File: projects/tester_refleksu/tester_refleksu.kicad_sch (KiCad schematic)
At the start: 25 parts, among them J1 +, J2 −, SW1 SW_Push_4P, SW2 SW_Push_4P, T1 BC548, T2 BC548, T3 BC557

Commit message: tester_refleksu_r2
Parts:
- added C3: 10μF, VeeCad:RA1_2, symbol Custom_Generic:C_Polarized
- added C4: 1nF, symbol *Custom_Generic:C
- added D4, D5: 4148, symbol *Custom_Generic:D
- added D7: 3V3, symbol *Custom_Generic:D_zener
- added R12, R15, R16: 10kΩ, VeeCad:AX3_1N, symbol Custom_Generic:R
- added R13, R14: 100kΩ, VeeCad:AX3_1N, symbol Custom_Generic:R
- added R17, R20, R21, R22: 1kΩ, VeeCad:AX3_1N, symbol Custom_Generic:R
- added R18, R19: 1kΩ, VeeCad:VERTAX_1N_180, symbol Custom_Generic:R
- added R23: 47kΩ, VeeCad:AX3_1N, symbol Custom_Generic:R
- added T4, T5, T6: 2n7000, symbol *Custom_Generic:NMOS_SGD
- added T7, T8, T9: BC548, VeeCad:TO92, symbol Custom_Generic:NPN_BJT_CBE
- added Y1: 3V, symbol *Custom_Generic:Buzzer_Magnetic_Active
- D1: value R -> Gr
- D2, D3: value Y -> Bl
- R8, R9: value 10kΩ -> 82kΩ
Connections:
- net GNDD: now also D7.2 (A), R17.1, R20.2, R21.2, T7.3 (E), T8.3 (E), Y1.2
- net VCC: now also R12.1, R13.1, R15.1, R22.2, T9.1 (C)
- net at D2.2 (A), D3.2 (A): now also R7.2; no longer R7.1
- net at R6.1, T3.1 (C): now also R7.1; no longer R7.2
- net at R10.2, TY2.2 (G): now also T4.1 (S); no longer SW2.1 (1A), SW2.3 (1B)
- net at R11.2, TY1.2 (G): now also T5.1 (S); no longer SW1.1 (1A), SW1.3 (1B)
- net at C2.2 (+), R4.2, T2.1 (C): now also R23.1
- new net: R23.2, T6.1 (S)
- new net: D4.1 (K), D5.1 (K), R21.1, T6.2 (G)
- new net: C4.2, T6.3 (D)
- new net: R19.2, SW2.1 (1A)
- new net: D5.2 (A), SW2.3 (1B)
- new net: R22.1, SW1.3 (1B), SW2.4 (2B)
- new net: D7.1 (K), R16.2, T9.2 (B)
- new net: T9.3 (E), Y1.1
- new net: R17.2, R18.1, T4.2 (G)
- new net: R9.1, T4.3 (D)
- new net: C3.1 (-), C4.1, R13.2, T8.2 (B)
- new net: R18.2, SW1.2 (2A)
- new net: D4.2 (A), SW1.4 (2B)
- new net: C3.2 (+), R12.2, T7.1 (C)
- new net: R14.2, R15.2, R16.1, T8.1 (C)
- new net: R8.2, T5.3 (D)
- new net: R14.1, T7.2 (B)
- new net: R19.1, R20.1, T5.2 (G)
- now unconnected: SW2.2 (2A)
- no-connect marks 0 -> 2
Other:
- note removed: "9...12V"
- moved on the sheet: C1, C2, D1, D2, D3, R1, R10, R11, R2, R3, R4, R5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

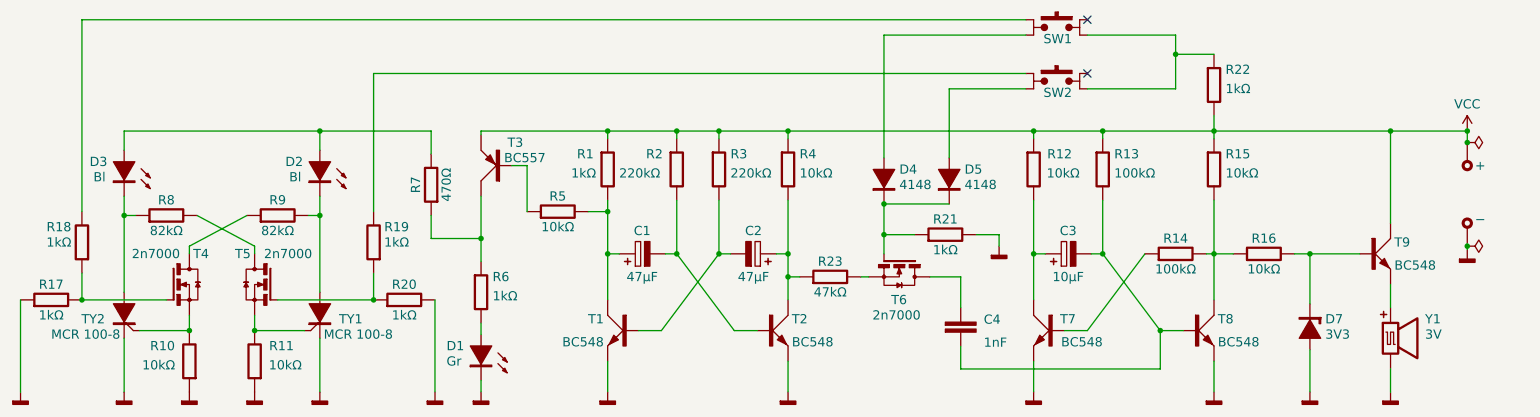
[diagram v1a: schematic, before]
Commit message: fixed buttons to trigger beeper on push not release
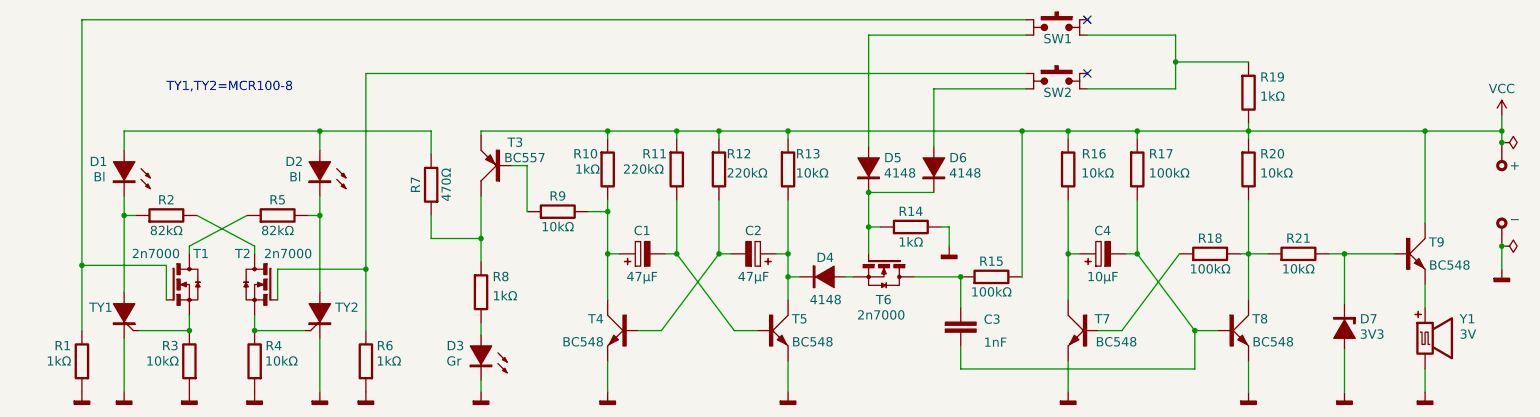
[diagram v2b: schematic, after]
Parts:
- removed R18, R19: 1kΩ, VeeCad:VERTAX_1N_180, symbol Custom_Generic:R
- removed R23: 47kΩ, VeeCad:AX3_1N, symbol Custom_Generic:R
- added D4: 4148, symbol *Custom_Generic:D
- added R15: 100kΩ, VeeCad:AX3_1N, symbol Custom_Generic:R
- renumbered C4 to C3, C3 to C4, D3 to D1, D1 to D3, D4 to D5, D5 to D6, R17 to R1, R1 to R10, R2 to R11, R3 to R12, R4 to R13, R21 to R14, R12 to R16, R13 to R17, R14 to R18, R22 to R19, R8 to R2, R15 to R20, R16 to R21, R10 to R3, R11 to R4, R9 to R5, R20 to R6, R6 to R8, R5 to R9, T4 to T1, T5 to T2, T1 to T4, T2 to T5, TY2 to TY1, TY1 to TY2
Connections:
- net GNDD: now also R6.1; no longer R6.2
- net VCC: now also R15.2
- net at T6.1 (S): now also D4.2 (A)
- net at C3.2, T6.3 (D): now also R15.1
- net at SW2.1 (1A): now also R6.2, T2.2 (G)
- net at R1.2, T1.2 (G): now also SW1.2 (2A)
- net at C2.2 (+), R13.2, T5.1 (C): now also D4.1 (K)
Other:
- note added: "TY1,TY2=MCR100-8"
- moved on the sheet: C4, D5, D6, D7, R1, R14, R16, R17, R18, R19, R20, R21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
